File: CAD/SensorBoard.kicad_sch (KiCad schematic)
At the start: 82 parts, among them J1 USB C 2.0, J2 SWD Connector, J3 UART Connector, J4 DAC Connector, M1 M1, M2 M2, M3 M3, M4 M4, SW1 SW_1, SW2 SW_2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

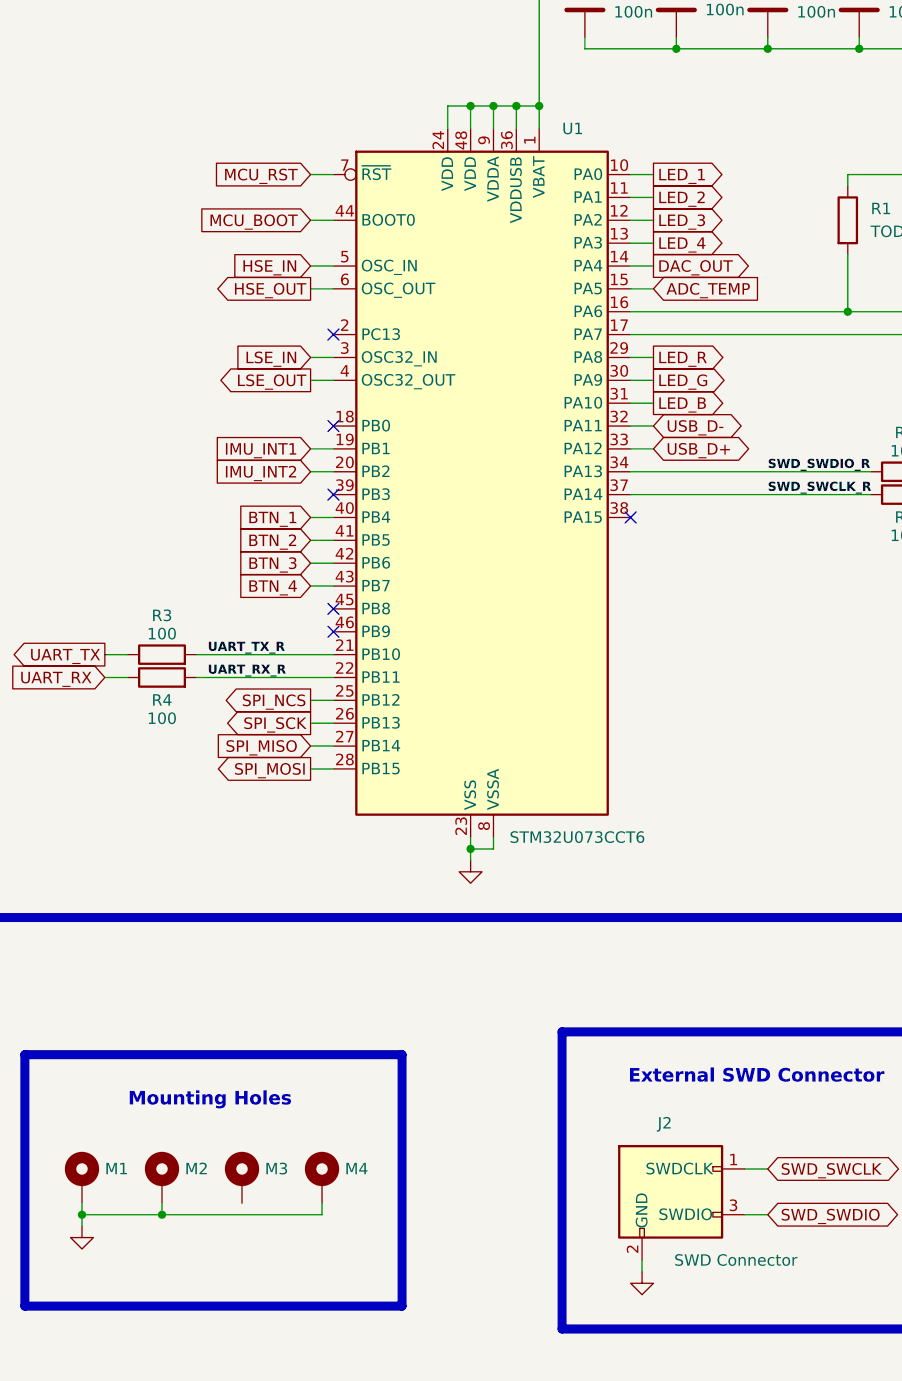
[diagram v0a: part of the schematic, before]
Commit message: Add initial traces and vias
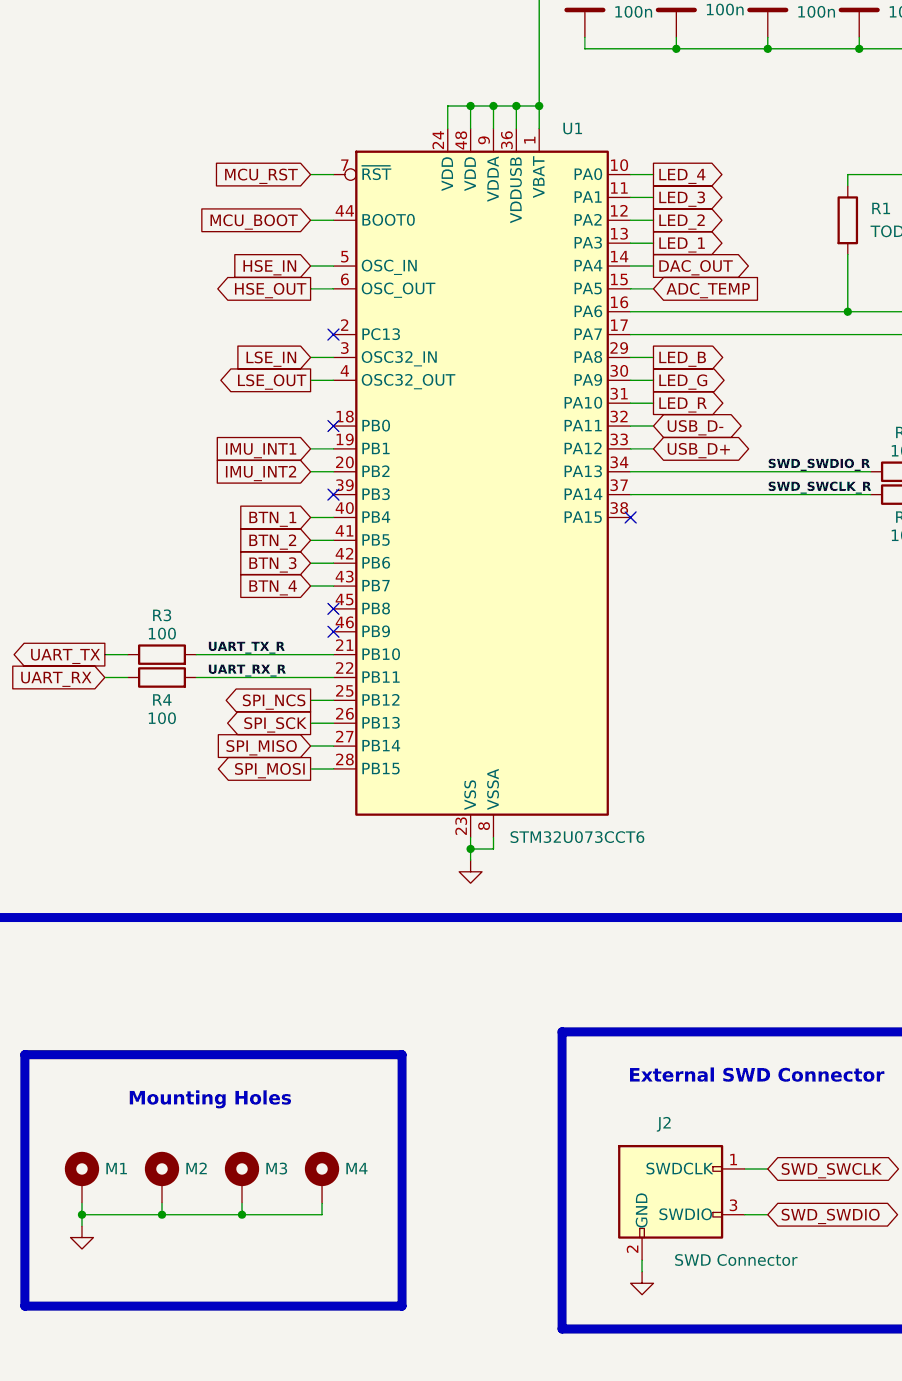
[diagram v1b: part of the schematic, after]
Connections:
- net GND: now also M3.1
- net LED_1: now also U1.13 (PA3); no longer U1.10 (PA0)
- net LED_2: now also U1.12 (PA2); no longer U1.11 (PA1)
- net LED_3: now also U1.11 (PA1); no longer U1.12 (PA2)
- net LED_4: now also U1.10 (PA0); no longer U1.13 (PA3)
- net LED_B: now also U1.29 (PA8); no longer U1.31 (PA10)
- net LED_R: now also U1.31 (PA10); no longer U1.29 (PA8)
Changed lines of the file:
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@@
 	)
 	(junction
+		(at 54.61 256.54)
+		(diameter 0)
+		(color 0 0 0 0)
+	)
+	(junction
 		(at 133.35 127)
 		(diameter 0)
@@
 	(wire
 		(pts
+			(xy 54.61 255.27) (xy 54.61 256.54)
+		)
+		(stroke
+			(width 0)
+			(type default)
+		)
+	)
+	(wire
+		(pts
 			(xy 360.68 60.96) (xy 360.68 68.58)
 		)
@@
 	(wire
 		(pts
+			(xy 54.61 256.54) (xy 45.72 256.54)
+		)
+		(stroke
+			(width 0)
+			(type default)
+		)
+	)
+	(wire
+		(pts
 			(xy 203.2 186.69) (xy 203.2 187.96)
 		)
@@
 	(wire
 		(pts
-			(xy 63.5 256.54) (xy 45.72 256.54)
+			(xy 63.5 256.54) (xy 54.61 256.54)
 		)
 		(stroke
@@
 		)
 	)
-	(global_label "LED_1"
+	(global_label "LED_4"
 		(shape output)
 		(at 100.33 140.97 0)
@@
 		)
 	)
-	(global_label "LED_2"
+	(global_label "LED_3"
 		(shape output)
 		(at 100.33 143.51 0)
@@
 		)
 	)
-	(global_label "LED_R"
+	(global_label "LED_B"
 		(shape output)
 		(at 100.33 161.29 0)
@@
 		)
 	)
-	(global_label "LED_B"
+	(global_label "LED_R"
 		(shape output)
 		(at 100.33 166.37 0)
@@
 		)
 	)
-	(global_label "LED_3"
+	(global_label "LED_2"
 		(shape output)
 		(at 100.33 146.05 0)
@@
 		)
 	)
-	(global_label "LED_4"
+	(global_label "LED_1"
 		(shape output)
 		(at 100.33 148.59 0)

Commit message: Update some placement of componenets and silkscreen
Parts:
- U6: footprint Package_TO_SOT_SMD:SOT-23 -> SensorBoard:SOT-23
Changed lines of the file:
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@@
 			)
 		)
-		(property "Footprint" "Package_TO_SOT_SMD:SOT-23"
+		(property "Footprint" "SensorBoard:SOT-23"
 			(at 300.736 237.236 0)
 			(effects

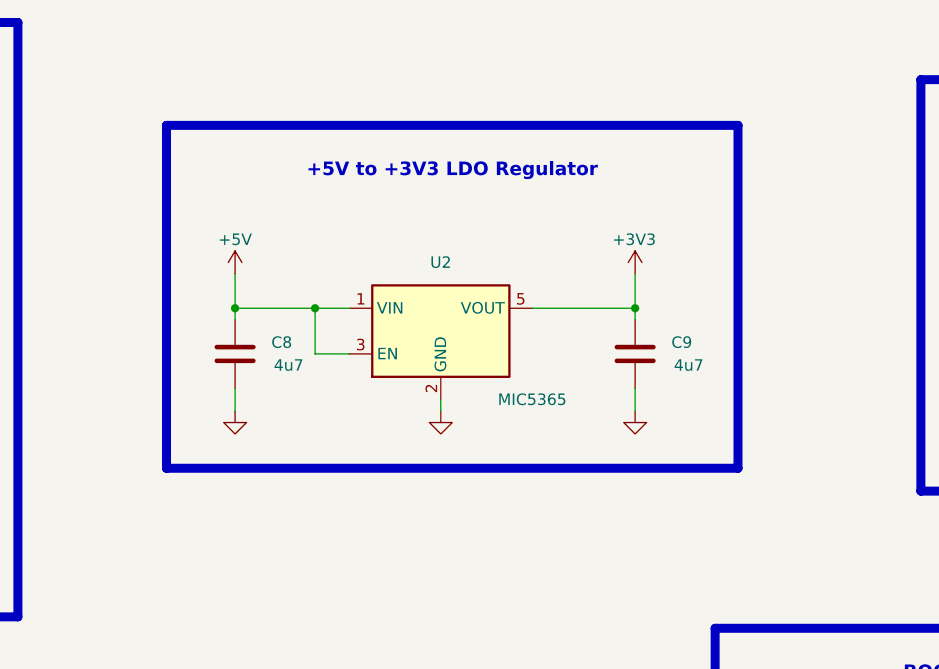
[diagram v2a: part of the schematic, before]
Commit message: Update LDO
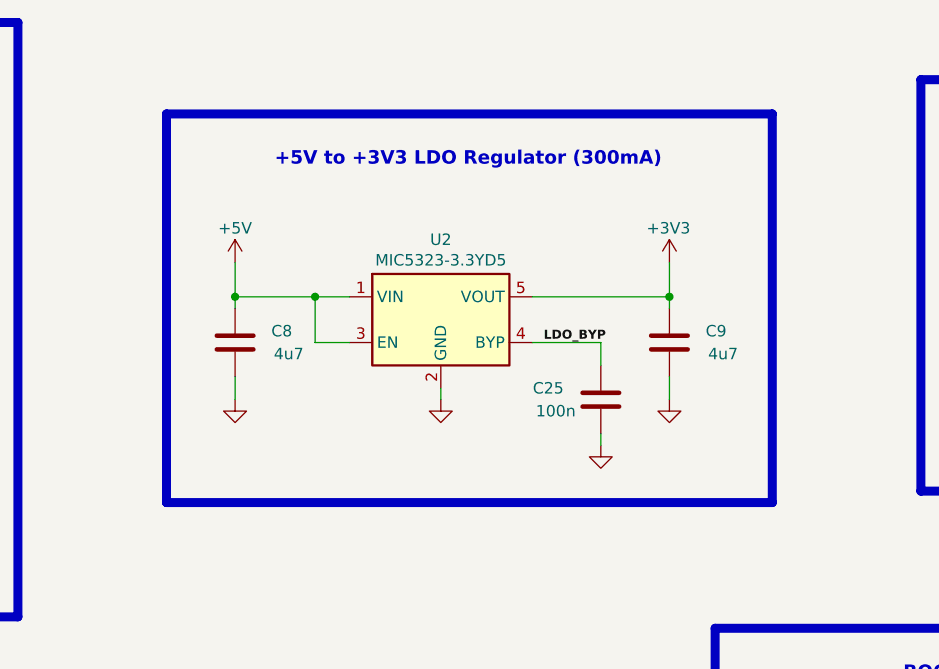
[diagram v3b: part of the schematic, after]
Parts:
- added C25: 100n, Capacitor_SMD:C_0603_1608Metric, symbol Device:C
- U2: value MIC5365 -> MIC5323-3.3YD5; footprint Package_TO_SOT_SMD:SOT-23-5 -> SensorBoard:SOT-23-5; symbol Regulator_Linear:MIC5365-3.3YD5 -> SensorBoard:MIC5365-3.3YD5
- U6: footprint SensorBoard:SOT-23 -> SensorBoard:SOT-23-3
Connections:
- net GND: now also C25.1
- net LDO_BYP: now reaches U2.4 (BYP)
- net LDO_BYP: now also C25.2
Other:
- note added: "+5V to +3V3 LDO Regulator (300mA)"
- note removed: "+5V to +3V3 LDO Regulator"
- moved on the sheet: C8, C9
